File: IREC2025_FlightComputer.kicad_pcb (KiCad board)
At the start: 4 copper layers, 165.2 x 176 mm, 125 parts, among them J1 Molex Microfit, J2 BOOT0, J3 Companion, J4 Molex Microfit, J5 SWD, J6 Molex Microfit, J8 MEM2080-00-128-00-A_REVA, Q1 SI7232DN-T1-GE3, U1 STM32U575VGTx, U10 XL4015E1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

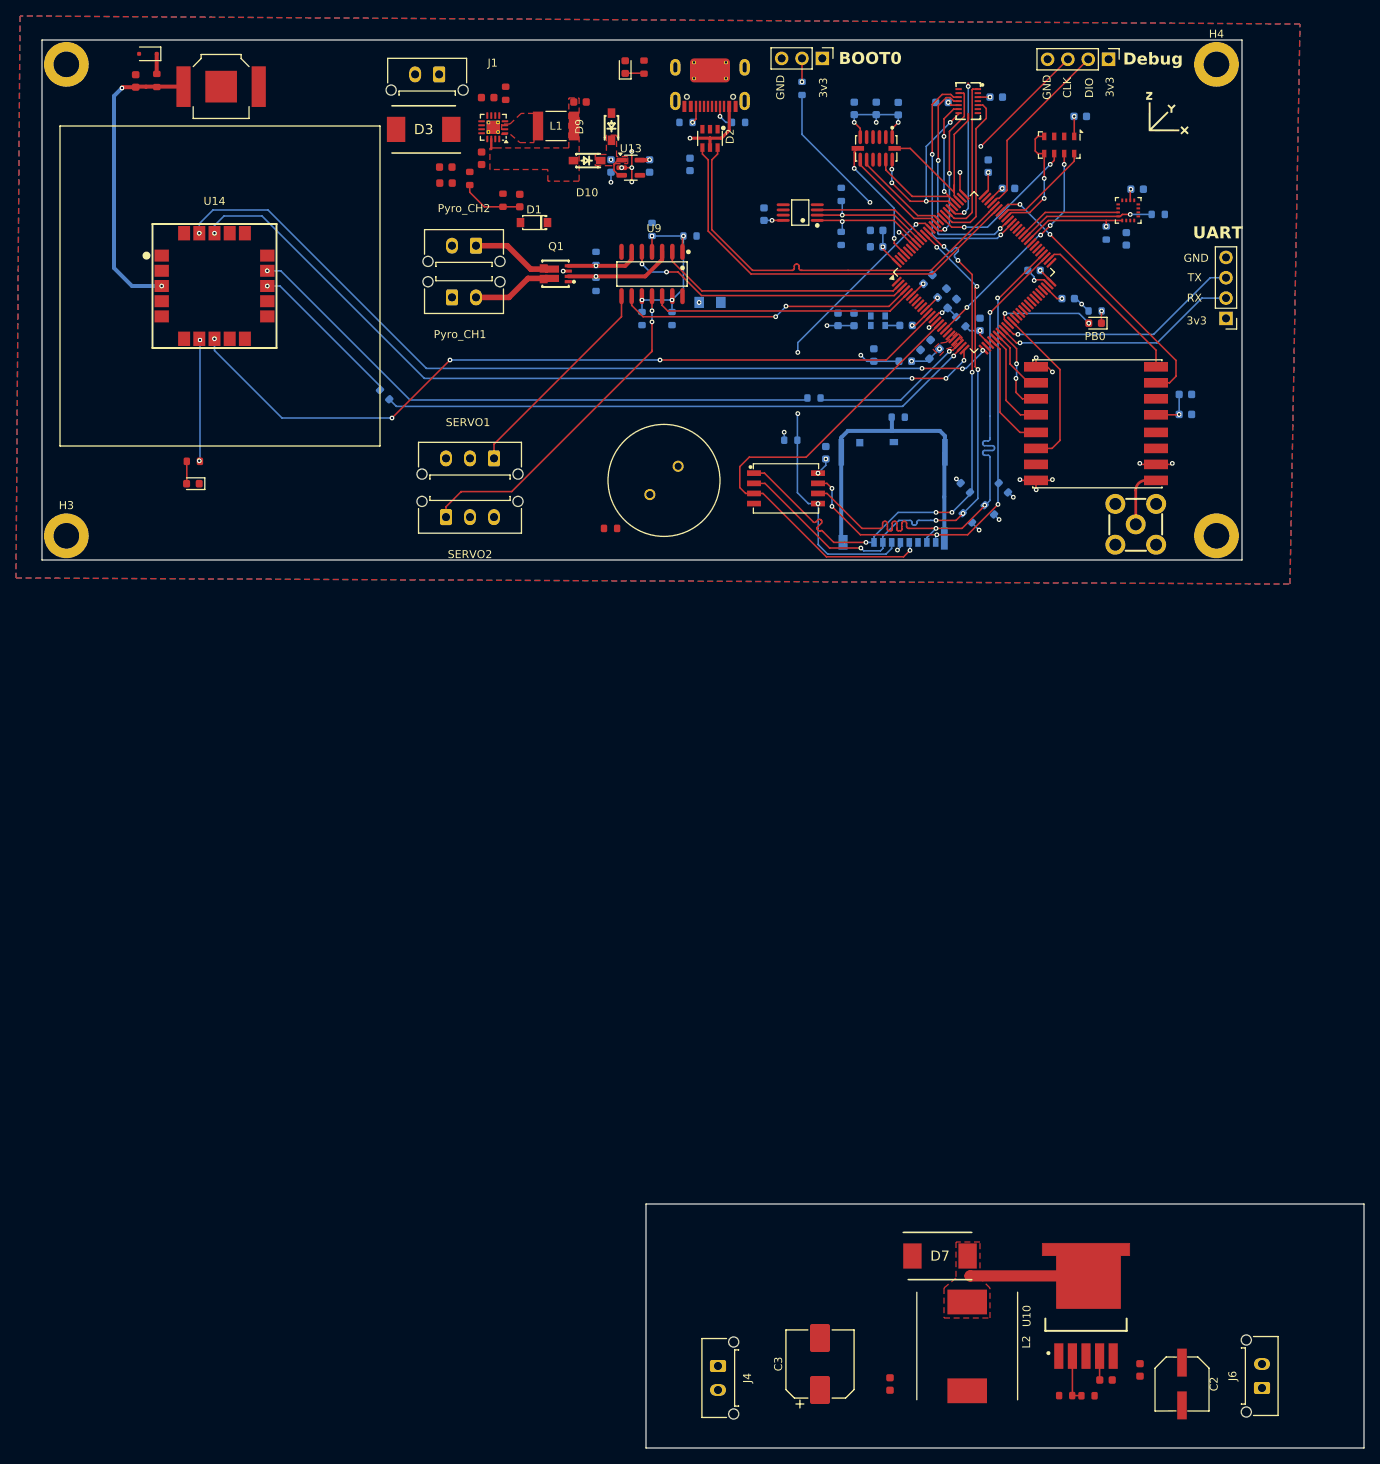
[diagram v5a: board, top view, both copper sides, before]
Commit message: Added silkscreen + Changed gps vbackup
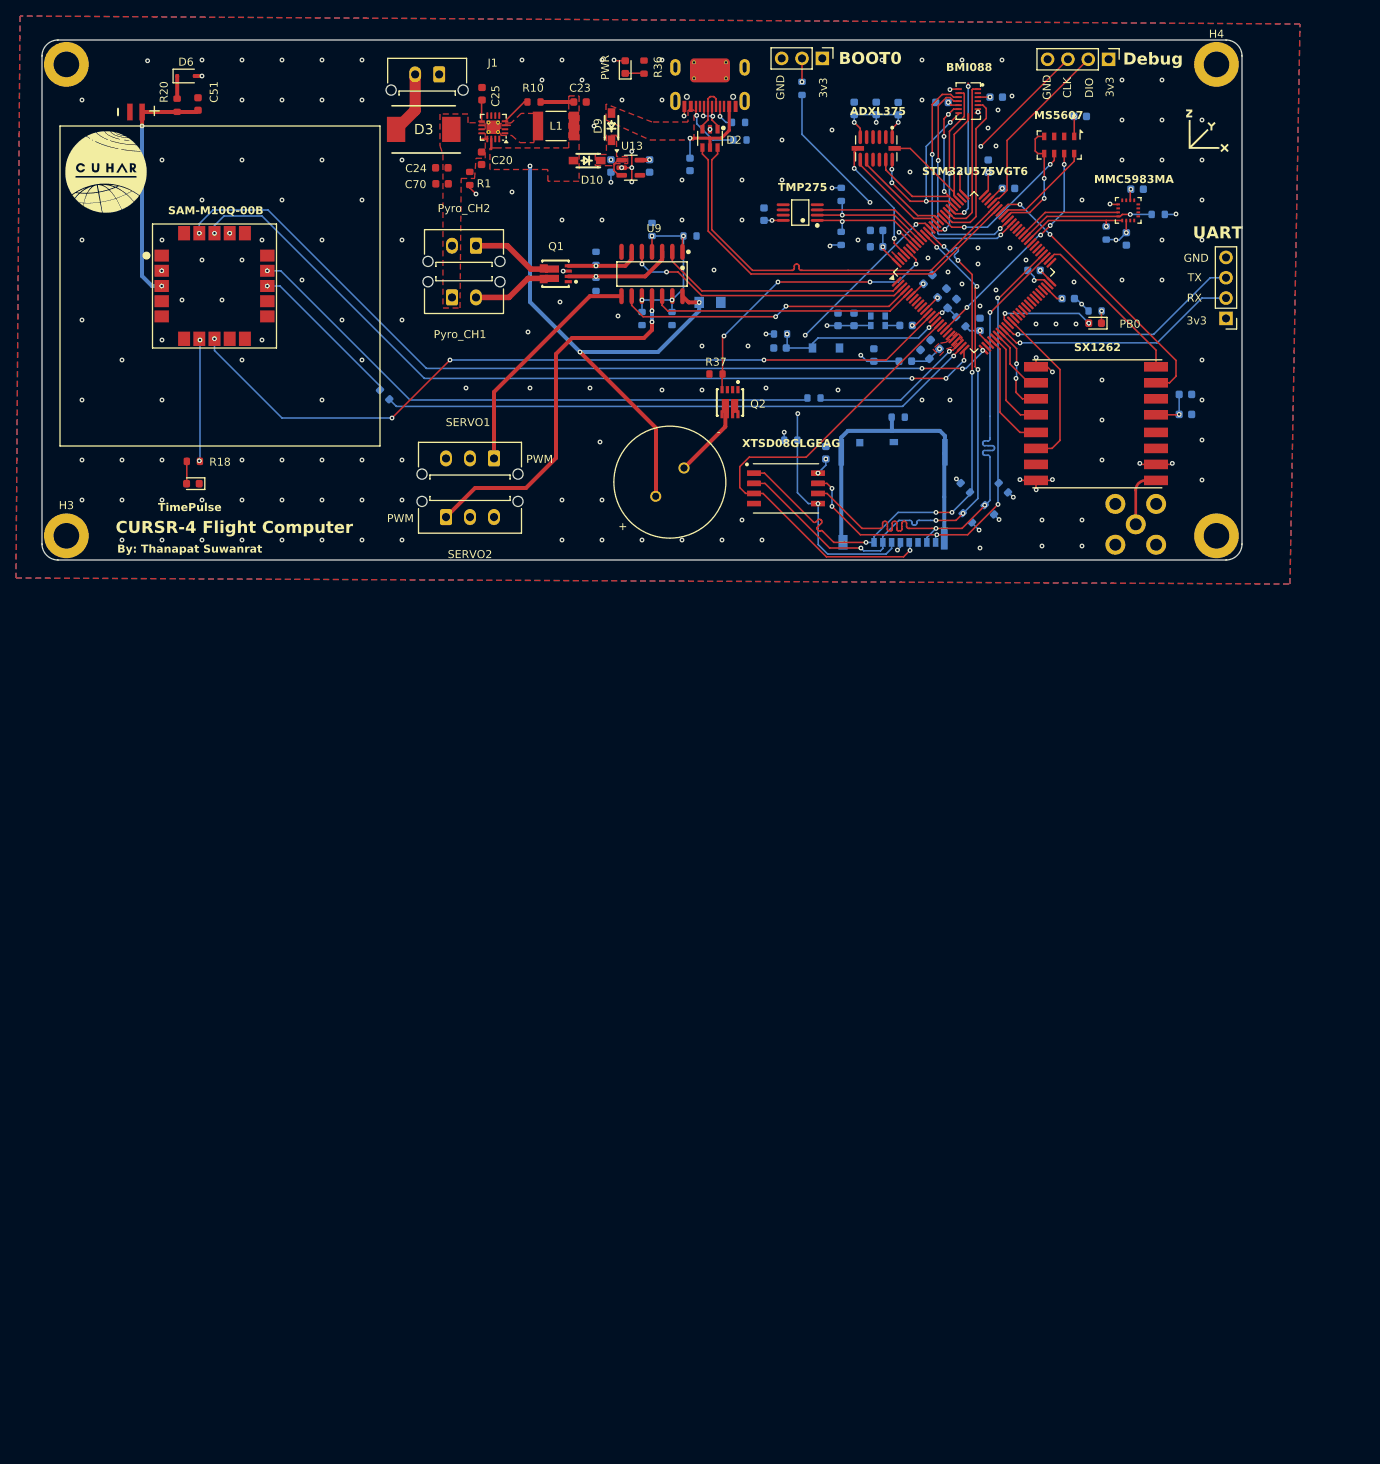
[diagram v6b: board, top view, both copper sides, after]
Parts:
- removed BT1: 3098, GNSS:BAT_3098
- removed C19: 1uF, PCM_JLCPCB:C_0603
- removed C2: 220UF 16V, EasyEDA:CAP-SMD_BD6.3-L6.6-W6.6-LS7.4-FD
- removed C29, C31: 100nF, PCM_JLCPCB:C_0603
- removed C3: 470uF, Capacitor_SMD:CP_Elec_8x10
- removed D7: SS34_C466502, GNSS:DIOM7959X262N
- removed J4, J6: Molex Microfit, Connector_Molex:Molex_Micro-Fit_3.0_43650-0215_1x02_P3.00mm_Vertical
- removed L2: 33uH,5A, Inductor_SMD:L_Bourns_SRR1208_12.7x12.7mm
- removed R24: 3.3kΩ, PCM_JLCPCB:R_0603
- removed R5: 1kΩ, PCM_JLCPCB:R_0603
- removed R8: 10kΩ, PCM_JLCPCB:R_0603
- removed U10: XL4015E1, EasyEDA:TO-263-5_L10.2-W8.9-P1.70-TL
- added LOGO: LOGO, Cuharlogo:CUHARLOGOMOD, F.Cu at (28.0, 85.5)
- added Q2: SI7232DN-T1-GE3, EasyEDA:POWER-1212-8_L3.3-W3.3-P0.66-LS3.3-BL, F.Cu at (106.0, 114.2)
- added R37: 47kΩ, PCM_JLCPCB:R_0603, F.Cu at (104.2, 110.8)
- added U5: MS621FE-FL11E, EasyEDA:BAT-SMD_FL11E, F.Cu at (31.8, 78.0)
- C17, D1, R2: moved to B.Cu
- L1: value 2.2uH,50mA -> 2.2uH,1A
- R16, R17: value 3.3kΩ -> 10kΩ
- moved D1 39.7 mm to (118.0, 107.5)
- moved R2 38.5 mm to (112.3, 105.8), turned to 180 degrees
- moved C17 37.4 mm to (112.2, 107.5), turned to 180 degrees
- moved C51 8.30 mm to (39.5, 77.0)
- moved R4 7.10 mm to (107.2, 81.5), turned to 180 degrees
- moved D6 5.51 mm to (38.0, 73.5), turned to 0 degrees
- moved G*** 5.46 mm to (165.8, 80.8)
- moved R20 4.01 mm to (36.9, 77.2)
- moved R10 3.70 mm to (81.5, 76.8), turned to 180 degrees
- moved C25 0.86 mm to (75.0, 75.7), turned to -90 degrees
- moved LS1 0.76 mm to (98.5, 124.3)
- moved C24 0.50 mm to (70.0, 85.0)
- moved C70 0.50 mm to (70.0, 87.0)
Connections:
- LS1 pad 1: BUZZER -> Net-(LS1-Pad1)
- LS1 pad 2: Net-(LS1-Pad2) -> +5V
- U1 pad 40: BUZZER -> unconnected-(U1-PE9-Pad40)
- U1 pad 96: unconnected-(U1-PB9-Pad96) -> BUZZER
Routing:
- net +5V: track 1.26 -> 73.7 mm, vias 1 -> 3
- net BAT_LEVEL: track 9.14 -> 69.8 mm, vias 1 -> 3
- net BUZZER: track 0.00 -> 36.6 mm, vias 0 -> 4
- net Net-(D7-Pad2): track 14.8 -> 0.00 mm
- net +3.3V: track 64.5 -> 78.5 mm, vias 26 -> 36
- net Net-(LS1-Pad1): track 0.00 -> 9.90 mm
- net Net-(J1-Pin_2): track 0.00 -> 7.86 mm
- net +5Vservo: track 0.00 -> 7.33 mm
- net Backup: track 37.6 -> 30.6 mm
- net D-: track 0.00 -> 6.27 mm
- net Net-(U10-FB): track 6.11 -> 0.00 mm
- net D+: track 0.00 -> 5.59 mm, vias 0 -> 2
- net Net-(USB1-CC2): track 2.18 -> 7.66 mm
- net SERVO_B: track 42.1 -> 47.3 mm
- net ADXL_MISO: track 24.1 -> 28.9 mm, vias 2 -> 4
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- added copper zone on F.Cu, net Net-(L1-Pad1)
- added copper zone on F.Cu, net VBAT+
- added copper zone on F.Cu, net VBUS
- removed copper zone on F.Cu, net (none)
- removed copper zone on F.Cu, net Net-(D7-Pad2)
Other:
- board size 165.2 x 176 mm -> 150 x 65 mm
- board text added: "+"
- board text added: "-"
- board text added: "ADXL375"
- board text added: "BMI088"
- board text added: "By: Thanapat Suwanrat"
- board text added: "CURSR-4 Flight Computer"
- board text added: "MMC5983MA"
- board text added: "MS5607"
- board text added: "PWM"
- board text added: "PWR"
- board text added: "SAM-M10Q-00B"
- board text added: "STM32U575VGT6"
- board text added: "SX1262"
- board text added: "TMP275"
- board text added: "TimePulse"
- board text added: "XTSD08GLGEAG"
